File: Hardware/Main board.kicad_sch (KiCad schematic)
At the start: 39 parts, among them J3 XT30PW-M, U1 ESP32-S3, Y1 R940000171

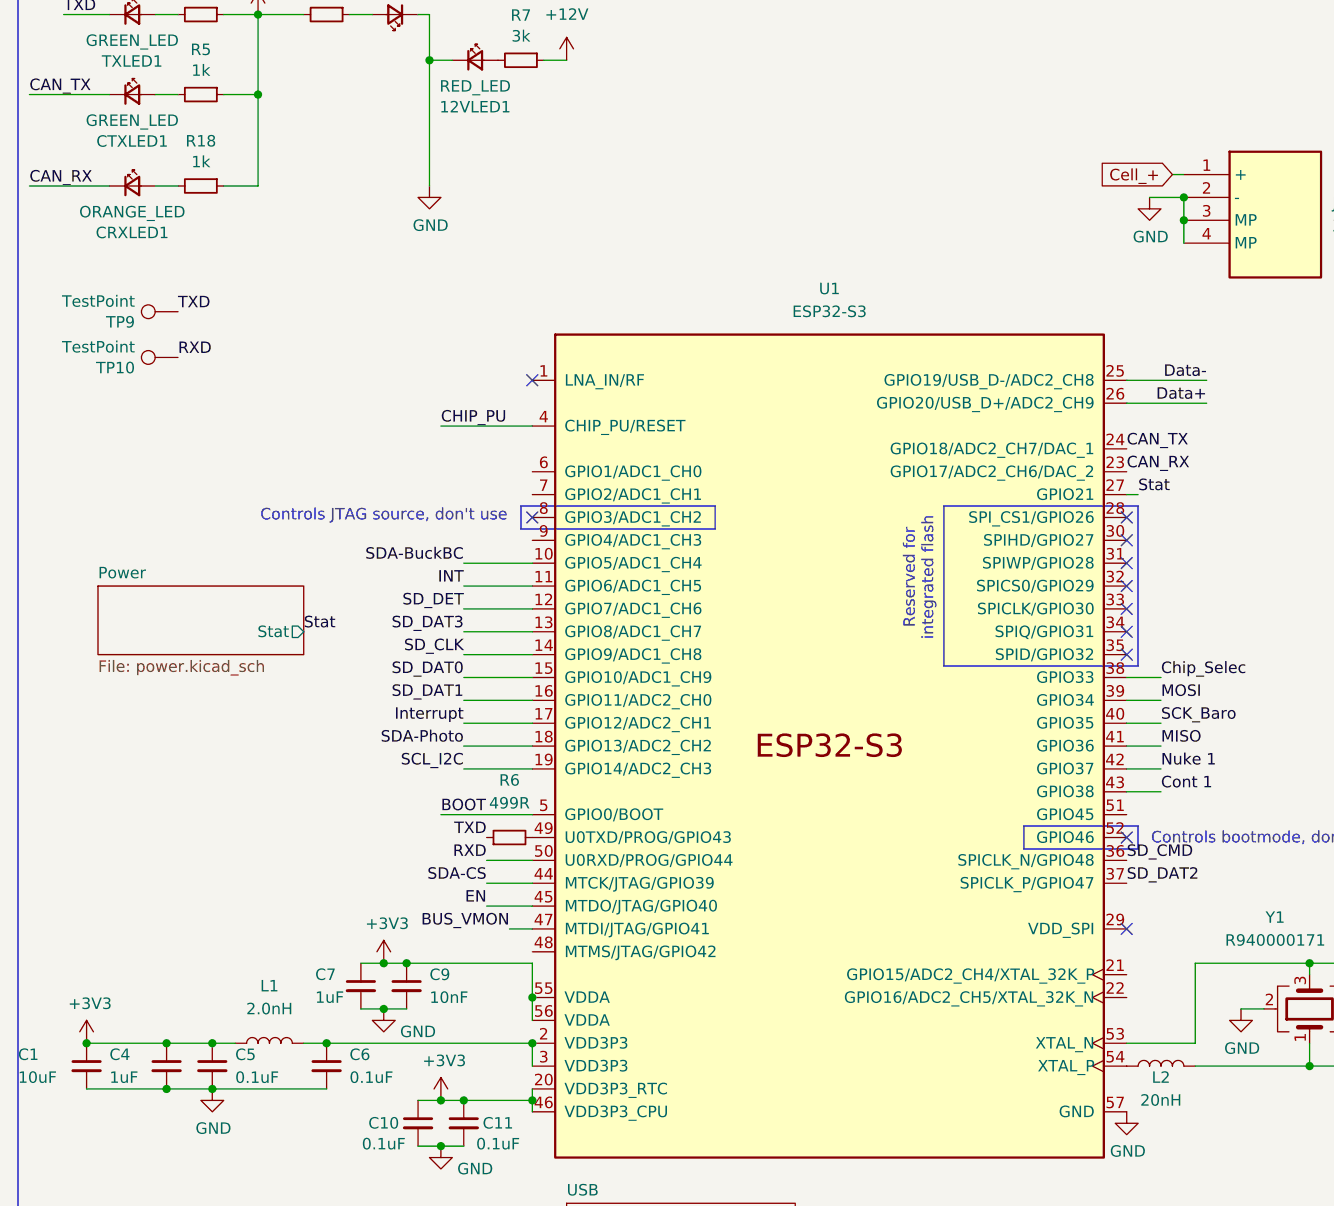
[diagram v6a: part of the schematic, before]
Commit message: Added MOSFET circuit to turn cell power on/off
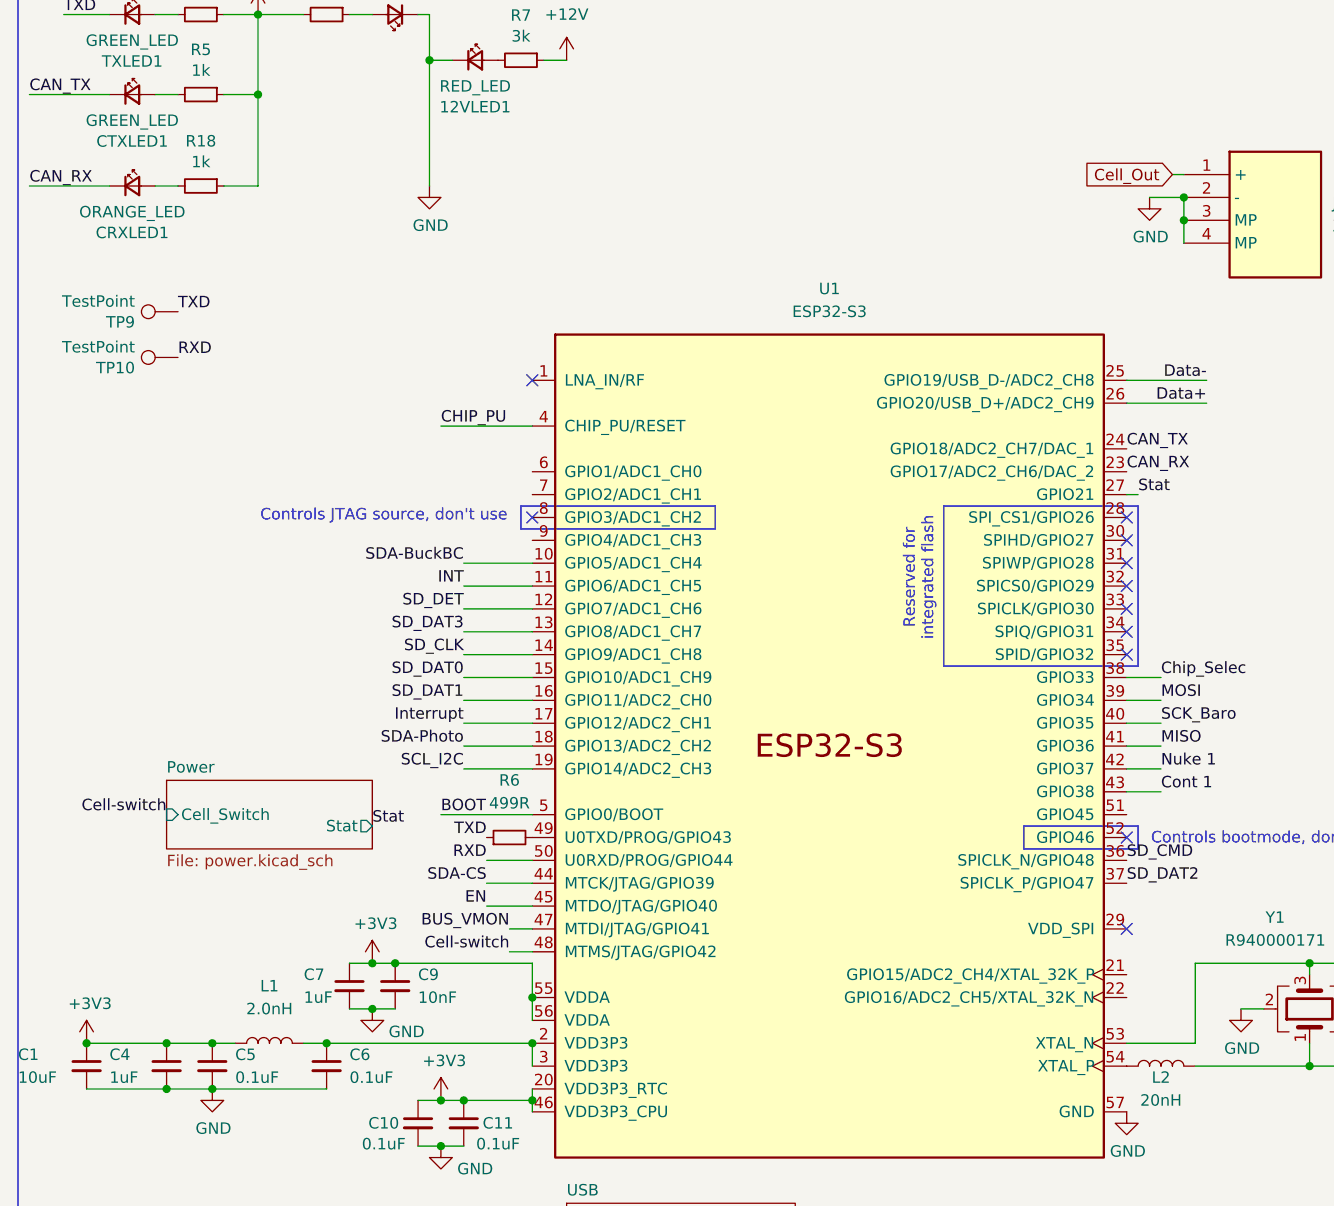
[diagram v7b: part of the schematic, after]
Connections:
- net Cell_+: no longer J3.1 (+)
- net Cell-switch: now reaches U1.48 (MTMS/JTAG/GPIO42)
- new net Cell_Out: J3.1 (+)
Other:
- sheet Power ports: added Cell_Switch; removed none
- moved on the sheet: C7, C9
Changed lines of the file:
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@@
 	)
 	(junction
-		(at 53.34 127)
-		(diameter 0)
-		(color 0 0 0 0)
-	)
-	(junction
 		(at 58.42 26.67)
 		(diameter 0)
@@
 	)
 	(junction
-		(at 55.88 127)
-		(diameter 0)
-		(color 0 0 0 0)
-	)
-	(junction
 		(at 63.5 165.1)
 		(diameter 0)
@@
 	)
 	(junction
+		(at 52.07 127)
+		(diameter 0)
+		(color 0 0 0 0)
+	)
+	(junction
 		(at 45.72 170.18)
 		(diameter 0)
@@
 	)
 	(junction
-		(at 53.34 132.08)
+		(at 156.21 138.43)
 		(diameter 0)
 		(color 0 0 0 0)
 	)
 	(junction
-		(at 156.21 138.43)
+		(at 69.85 130.81)
 		(diameter 0)
 		(color 0 0 0 0)
 	)
 	(junction
-		(at 69.85 130.81)
+		(at 29.21 140.97)
 		(diameter 0)
 		(color 0 0 0 0)
 	)
 	(junction
-		(at 29.21 140.97)
+		(at 52.07 132.08)
 		(diameter 0)
 		(color 0 0 0 0)
@@
 	)
 	(junction
+		(at 54.61 127)
+		(diameter 0)
+		(color 0 0 0 0)
+	)
+	(junction
 		(at 270.51 33.02)
 		(diameter 0)
@@
 		)
 	)
+	(wire
+		(pts
+			(xy 52.07 127) (xy 54.61 127)
+		)
+		(stroke
+			(width 0)
+			(type default)
+		)
+	)
 	(polyline
 		(pts
@@
 	(wire
 		(pts
+			(xy 67.31 125.73) (xy 69.85 125.73)
+		)
+		(stroke
+			(width 0)
+			(type default)
+		)
+	)
+	(wire
+		(pts
 			(xy 16.51 191.77) (xy 20.32 191.77)
 		)
@@
 	(wire
 		(pts
-			(xy 53.34 132.08) (xy 55.88 132.08)
-		)
-		(stroke
-			(width 0)
-			(type default)
-		)
-	)
-	(wire
-		(pts
 			(xy 143.51 135.89) (xy 143.51 127)
 		)
@@
 	(wire
 		(pts
-			(xy 50.8 132.08) (xy 53.34 132.08)
+			(xy 49.53 132.08) (xy 52.07 132.08)
 		)
 		(stroke
@@
 	(wire
 		(pts
-			(xy 50.8 127) (xy 53.34 127)
+			(xy 49.53 127) (xy 52.07 127)
 		)
 		(stroke
@@
 	(wire
 		(pts
-			(xy 219.71 120.65) (xy 222.25 120.65)
+			(xy 52.07 132.08) (xy 54.61 132.08)
 		)
 		(stroke
@@
 	(wire
 		(pts
-			(xy 29.21 140.97) (xy 34.29 140.97)
+			(xy 219.71 120.65) (xy 222.25 120.65)
 		)
 		(stroke
@@
 	(wire
 		(pts
-			(xy 35.56 21.59) (xy 39.37 21.59)
+			(xy 29.21 140.97) (xy 34.29 140.97)
 		)
 		(stroke
@@
 	(wire
 		(pts
-			(xy 55.88 127) (xy 69.85 127)
+			(xy 35.56 21.59) (xy 39.37 21.59)
 		)
 		(stroke
@@
 	(wire
 		(pts
+			(xy 54.61 127) (xy 69.85 127)
+		)
+		(stroke
+			(width 0)
+			(type default)
+		)
+	)
+	(wire
+		(pts
 			(xy 59.69 67.31) (xy 69.85 67.31)
 		)
@@
 	(wire
 		(pts
-			(xy 53.34 127) (xy 55.88 127)
-		)
-		(stroke
-			(width 0)
-			(type default)
-		)
-	)
-	(wire
-		(pts
 			(xy 62.23 100.33) (xy 69.85 100.33)
 		)
@@
 		)
 	)
+	(label "Cell-switch"
+		(at 67.31 125.73 180)
+		(effects
+			(font
+				(size 1.27 1.27)
+			)
+			(justify right bottom)
+		)
+	)
 	(label "PyroPWR"
 		(at 201.93 59.69 180)
@@
 	)
 	(label "Stat"
-		(at 44.45 90.17 0)
+		(at 52.07 111.76 0)
 		(effects
 			(font
@@
 		)
 	)
+	(label "Cell-switch"
+		(at 29.21 110.49 180)
+		(effects
+			(font
+				(size 1.27 1.27)
+			)
+			(justify right bottom)
+		)
+	)
 	(label "RXD"
 		(at 64.77 115.57 180)
@@
 		)
 	)
-	(global_label "Cell_+"
+	(global_label "Cell_Out"
 		(shape input)
 		(at 140.97 39.37 180)
@@
 		)
 		(property "Intersheetrefs" "${INTERSHEET_REFS}"
-			(at 132.41 39.37 0)
+			(at 130.7772 39.37 0)
 			(effects
 				(font
@@
 	(symbol
 		(lib_id "Device:C_Small")
-		(at 55.88 129.54 0)
+		(at 54.61 129.54 0)
 		(unit 1)
 		(exclude_from_sim no)
@@
 		(fields_autoplaced yes)
 		(property "Reference" "C9"
-			(at 58.42 128.2762 0)
+			(at 57.15 128.2762 0)
 			(effects
 				(font
@@
 		)
 		(property "Value" "10nF"
-			(at 58.42 130.8162 0)
+			(at 57.15 130.8162 0)
 			(effects
 				(font
@@
 		)
 		(property "Footprint" "Capacitor_SMD:C_0402_1005Metric"
-			(at 55.88 129.54 0)
+			(at 54.61 129.54 0)
 			(effects
 				(font
@@
 		)
 		(property "Datasheet" "~"
-			(at 55.88 129.54 0)
+			(at 54.61 129.54 0)
 			(effects
 				(font
@@
 		)
 		(property "Description" ""
-			(at 55.88 129.54 0)
+			(at 54.61 129.54 0)
 			(effects
 				(font
@@
 	(symbol
 		(lib_id "power:+3.3V")
-		(at 53.34 127 0)
+		(at 52.07 127 0)
 		(unit 1)
 		(exclude_from_sim no)
@@
 		(dnp no)
 		(property "Reference" "#PWR010"
-			(at 53.34 130.81 0)
+			(at 52.07 130.81 0)
 			(effects
 				(font
@@
 		)
 		(property "Value" "+3V3"
-			(at 53.721 122.6058 0)
+			(at 52.451 122.6058 0)
 			(effects
 				(font
@@
 		)
 		(property "Footprint" ""
-			(at 53.34 127 0)
+			(at 52.07 127 0)
 			(effects
 				(font
@@
 		)
 		(property "Datasheet" ""
-			(at 53.34 127 0)
+			(at 52.07 127 0)
 			(effects
 				(font
@@
 		)
 		(property "Description" ""
-			(at 53.34 127 0)
+			(at 52.07 127 0)
 			(effects
 				(font
@@
 	(symbol
 		(lib_id "Device:C_Small")
-		(at 50.8 129.54 0)
+		(at 49.53 129.54 0)
 		(unit 1)
 		(exclude_from_sim no)
@@
 		(dnp no)
 		(property "Reference" "C7"
-			(at 45.72 128.27 0)
+			(at 44.45 128.27 0)
 			(effects
 				(font
@@
 		)
 		(property "Value" "1uF"
-			(at 45.72 130.81 0)
+			(at 44.45 130.81 0)
 			(effects
 				(font
@@
 		)
 		(property "Footprint" "Capacitor_SMD:C_0402_1005Metric"
-			(at 50.8 129.54 0)
+			(at 49.53 129.54 0)
 			(effects
 				(font
@@
 		)
 		(property "Datasheet" "~"
-			(at 50.8 129.54 0)
+			(at 49.53 129.54 0)
 			(effects
 				(font
@@
 		)
 		(property "Description" ""
-			(at 50.8 129.54 0)
+			(at 49.53 129.54 0)
 			(effects
 				(font
@@
 	(symbol
 		(lib_id "power:GND")
-		(at 53.34 132.08 0)
+		(at 52.07 132.08 0)
 		(unit 1)
 		(exclude_from_sim no)
@@
 		(dnp no)
 		(property "Reference" "#PWR011"
-			(at 53.34 138.43 0)
+			(at 52.07 138.43 0)
 			(effects
 				(font
@@
 		)
 		(property "Value" "GND"
-			(at 57.15 134.62 0)
+			(at 55.88 134.62 0)
 			(effects
 				(font
@@
 		)
 		(property "Footprint" ""
-			(at 53.34 132.08 0)
+			(at 52.07 132.08 0)
 			(effects
 				(font
@@
 		)
 		(property "Datasheet" ""
-			(at 53.34 132.08 0)
+			(at 52.07 132.08 0)
 			(effects
 				(font
@@
 		)
 		(property "Description" ""
-			(at 53.34 132.08 0)
+			(at 52.07 132.08 0)
 			(effects
 				(font
@@
 	)
 	(sheet
-		(at 21.59 85.09)
+		(at 29.21 106.68)
 		(size 22.86 7.62)
 		(exclude_from_sim no)
@@
 		)
 		(property "Sheetname" "Power"
-			(at 21.59 84.3784 0)
+			(at 29.21 105.9684 0)
 			(effects
 				(font
@@
 		)
 		(property "Sheetfile" "power.kicad_sch"
-			(at 21.59 93.2946 0)
+			(at 29.21 114.8846 0)
 			(effects
 				(font
@@
 		)
 		(pin "Stat" output
-			(at 44.45 90.17 0)
+			(at 52.07 111.76 0)
 			(effects
 				(font
@@
 			)
 		)
+		(pin "Cell_Switch" input
+			(at 29.21 110.49 180)
+			(effects
+				(font
+					(size 1.27 1.27)
+				)
+				(justify left)
+			)
+		)

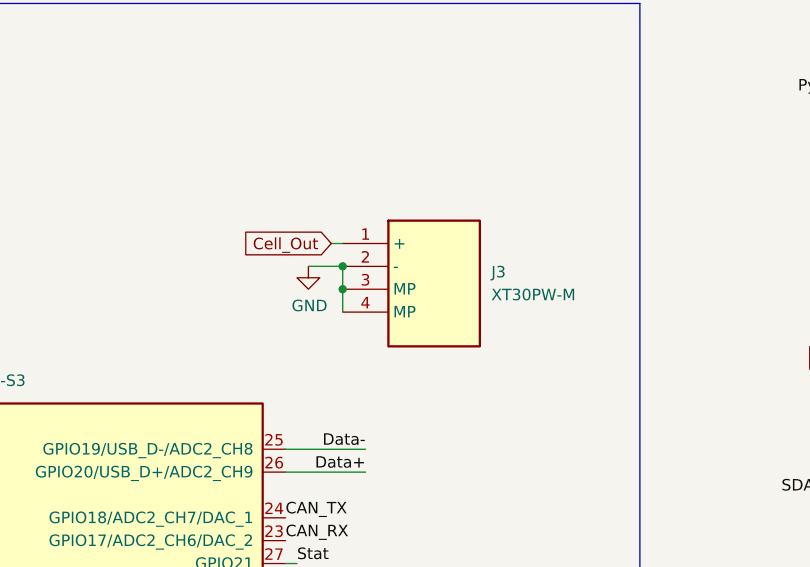
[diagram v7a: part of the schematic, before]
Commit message: Crosshair post review 2
Layout redesign + changes implemented. Traces not yet complete
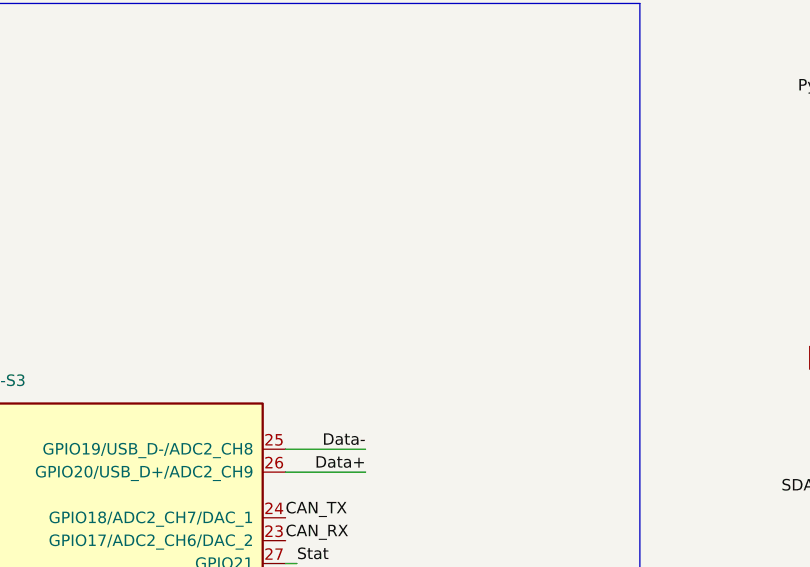
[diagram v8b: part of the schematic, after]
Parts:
- removed J3: XT30PW-M, iclr:XT30PWM, symbol iclr:XT30PW-M
